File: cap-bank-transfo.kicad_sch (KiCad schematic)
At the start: 25 parts, among them J1 Screw_Terminal_01x02, J2 Screw_Terminal_01x02, J3 Screw_Terminal_01x02, T1 FS28-420

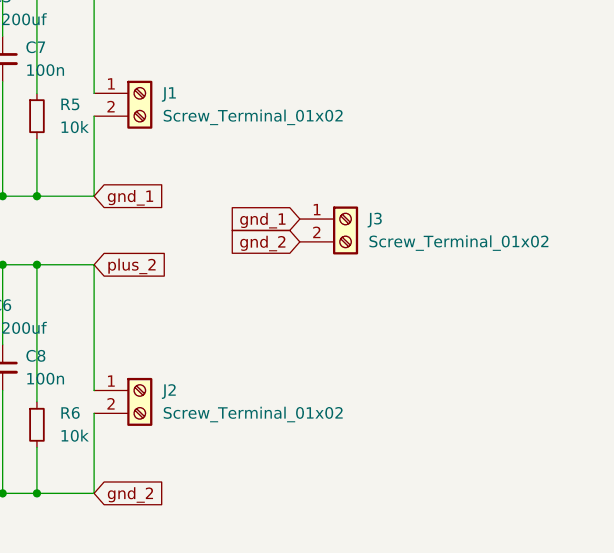
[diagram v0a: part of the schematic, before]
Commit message: added second header for ground jumpers
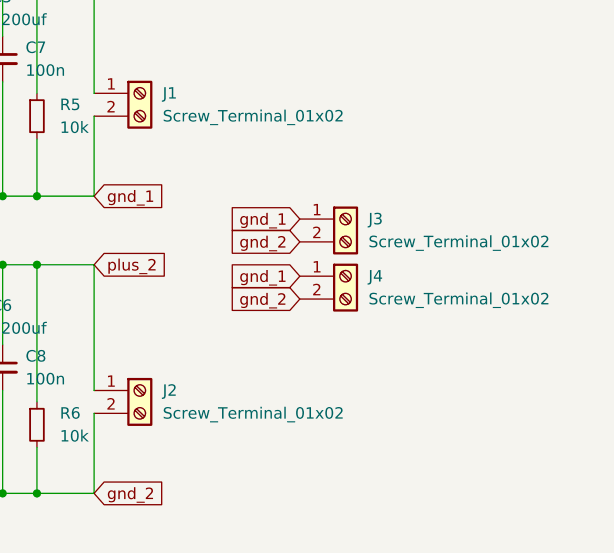
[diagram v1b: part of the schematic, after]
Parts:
- added J4: Screw_Terminal_01x02, Connector_PinHeader_2.54mm:PinHeader_1x02_P2.54mm_Vertical, symbol Connector:Screw_Terminal_01x02
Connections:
- net gnd_1: now also J4.1 (Pin_1)
- net gnd_2: now also J4.2 (Pin_2)
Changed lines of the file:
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@@
+		)
+	)
+	(global_label "gnd_2"
+		(shape input)
+		(at 176.53 90.17 180)
+		(fields_autoplaced yes)
+		(effects
+			(font
+				(size 1.27 1.27)
+			)
+			(justify right)
+		)
+		(property "Intersheetrefs" "${INTERSHEET_REFS}"
+			(at 167.9207 90.17 0)
+			(effects
+				(font
+					(size 1.27 1.27)
+				)
+				(justify right)
+				(hide yes)
+			)
 		)
 	)
@@
 		)
 	)
+	(global_label "gnd_1"
+		(shape input)
+		(at 176.53 87.63 180)
+		(fields_autoplaced yes)
+		(effects
+			(font
+				(size 1.27 1.27)
+			)
+			(justify right)
+		)
+		(property "Intersheetrefs" "${INTERSHEET_REFS}"
+			(at 167.9207 87.63 0)
+			(effects
+				(font
+					(size 1.27 1.27)
+				)
+				(justify right)
+				(hide yes)
+			)
+		)
+	)
 	(symbol
 		(lib_id "Device:R_Small")
@@
 					(unit 1)
 				)
+			)
+		)
+	)
+	(symbol
+		(lib_id "Connector:Screw_Terminal_01x02")
+		(at 181.61 87.63 0)
+		(unit 1)
+		(exclude_from_sim no)
+		(in_bom yes)
+		(on_board yes)
+		(dnp no)
+		(fields_autoplaced yes)
+		(property "Reference" "J4"
+			(at 184.15 87.6299 0)
+			(effects
+				(font
+					(size 1.27 1.27)
+				)
+				(justify left)
+			)
+		)
+		(property "Value" "Screw_Terminal_01x02"
+			(at 184.15 90.1699 0)
+			(effects
+				(font
+					(size 1.27 1.27)
+				)
+				(justify left)
+			)
+		)
+		(property "Footprint" "Connector_PinHeader_2.54mm:PinHeader_1x02_P2.54mm_Vertical"
+			(at 181.61 87.63 0)
+			(effects
+				(font
+					(size 1.27 1.27)
+				)
+				(hide yes)
+			)
+		)
+		(property "Datasheet" "~"
+			(at 181.61 87.63 0)
+			(effects
+				(font
+					(size 1.27 1.27)
+				)
+				(hide yes)
+			)
+		)
+		(property "Description" "Generic screw terminal, single row, 01x02, script generated (kicad-library-utils/schlib/autogen/connector/)"
+			(at 181.61 87.63 0)
+			(effects
+				(font
+					(size 1.27 1.27)
+				)
+				(hide yes)
+			)
+		)
+		(pin "1"
+		)
+		(pin "2"
+		)
+		(instances
+			(project "cap-bank-transfo"
+				(path "/08838421-4371-4c5b-b465-42e5d2dded23"
+					(reference "J4")
+					(unit 1)
+				)
